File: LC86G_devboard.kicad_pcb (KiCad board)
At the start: 4 copper layers, 35 x 35 mm, 19 parts, among them J2 U.FL-R-SMT_10_, J3 Conn_01x10_Pin, Q1 DTC143Z, Q2 DTC143Z, Q3 AO3415, U1 LC86G, U2 XC6206P332MR

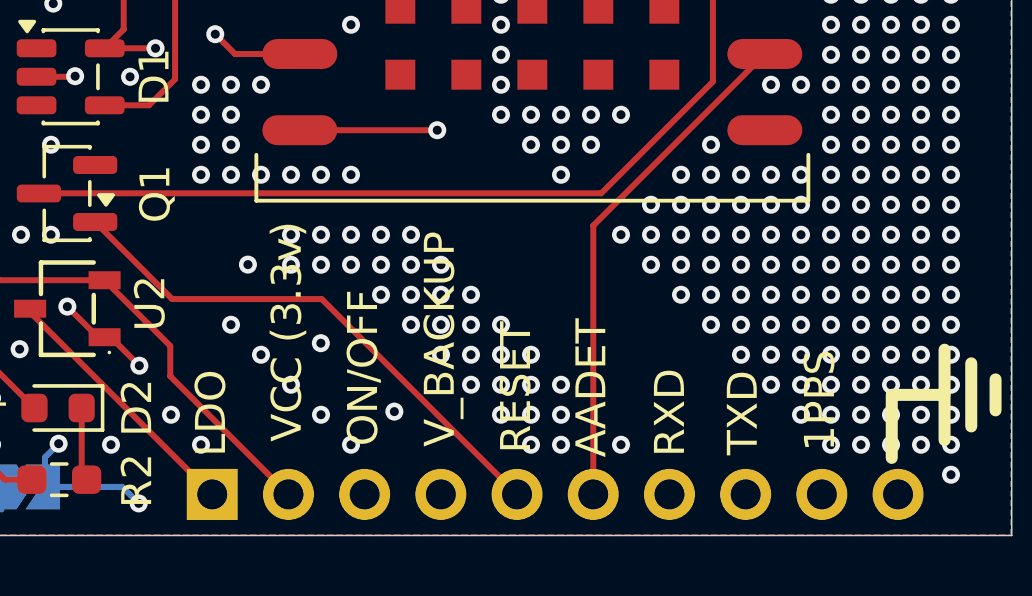
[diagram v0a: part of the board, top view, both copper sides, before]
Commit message: cambio de etiquetas
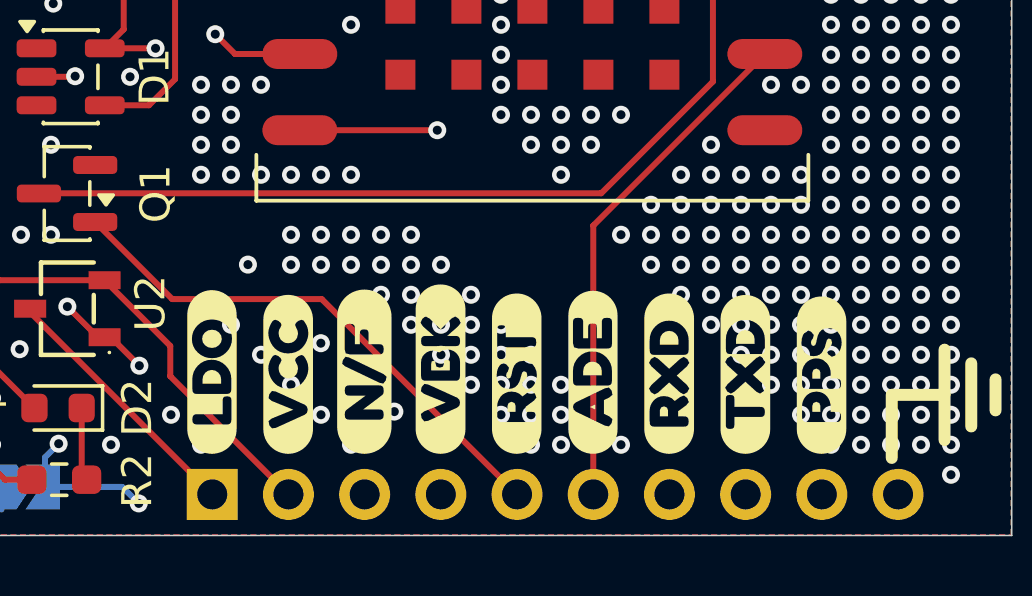
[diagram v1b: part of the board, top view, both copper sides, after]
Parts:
- added kibuzzard-6A7817EE: G***, kibuzzard-6A7817EE, F.Cu at (154.0, 105.1)
- added kibuzzard-6A781809: G***, kibuzzard-6A781809, F.Cu at (156.6, 105.0)
- added kibuzzard-6A781813: G***, kibuzzard-6A781813, F.Cu at (159.1, 104.9)
- added kibuzzard-6A78181D: G***, kibuzzard-6A78181D, F.Cu at (161.7, 105.0)
- added kibuzzard-6A78183E: G***, kibuzzard-6A78183E, F.Cu at (164.2, 105.0)
- added kibuzzard-6A781856: G***, kibuzzard-6A781856, F.Cu at (166.7, 105.0)
- added kibuzzard-6A781867: G***, kibuzzard-6A781867, F.Cu at (169.3, 105.1)
- added kibuzzard-6A78187E: G***, kibuzzard-6A78187E, F.Cu at (171.8, 105.1)
- added kibuzzard-6A781898: G***, kibuzzard-6A781898, F.Cu at (151.5, 105.0)
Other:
- board text removed: "1PPS"
- board text removed: "AADET"
- board text removed: "LDO"
- board text removed: "ON/OFF"
- board text removed: "RESET"
- board text removed: "RXD"
- board text removed: "TXD"
- board text removed: "VCC (3.3v)"
- board text removed: "V_BACKUP"
